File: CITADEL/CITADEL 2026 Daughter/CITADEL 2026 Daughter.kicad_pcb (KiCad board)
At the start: 2 copper layers, 36 x 36 mm, 4 parts

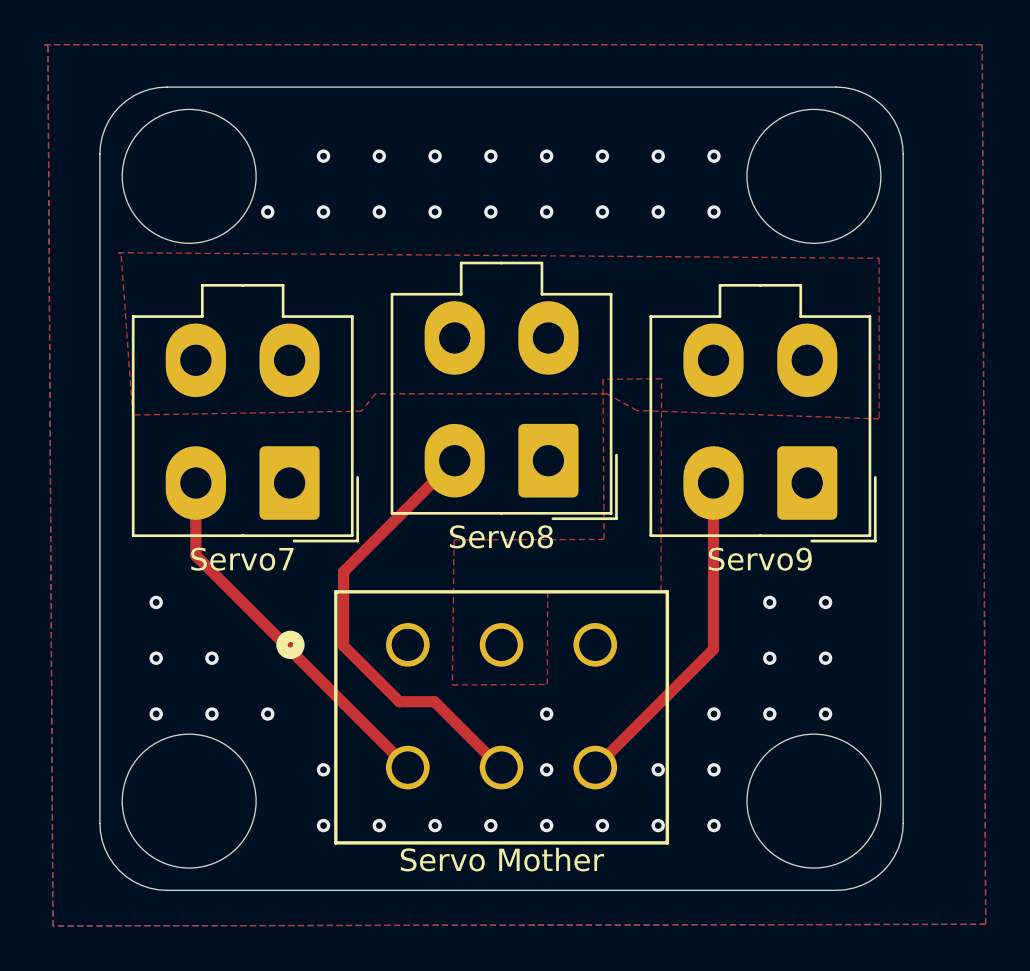
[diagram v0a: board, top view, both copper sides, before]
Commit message: Changed layout to support new linear actuators
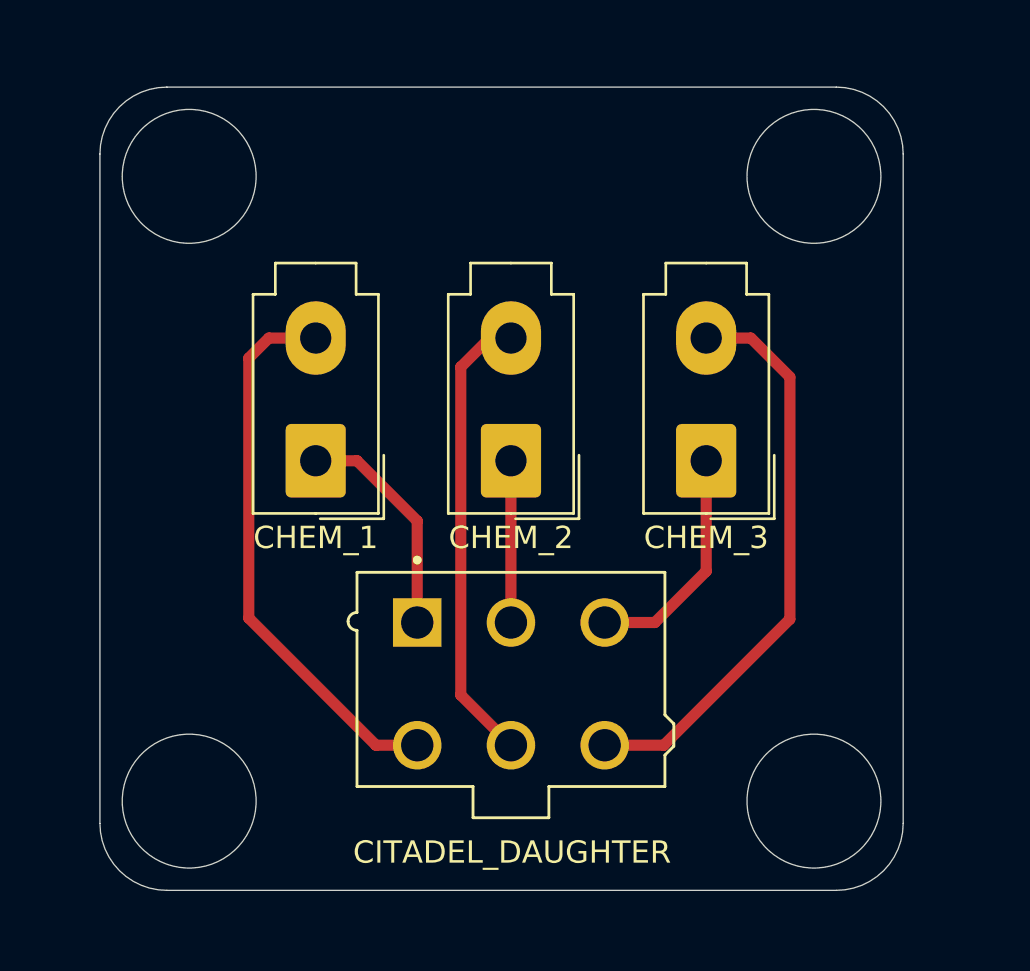
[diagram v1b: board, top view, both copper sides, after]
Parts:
- removed Servo7, Servo8, Servo9: Motor_Servo, Connector_Molex:Molex_Mini-Fit_Jr_5566-04A_2x02_P4.20mm_Vertical
- added CHEM_1: CHEM_1, Connector_Molex:Molex_Mini-Fit_Jr_5566-02A_2x01_P4.20mm_Vertical, F.Cu at (35.0, 38.4)
- added CHEM_2: CHEM_2, Connector_Molex:Molex_Mini-Fit_Jr_5566-02A_2x01_P4.20mm_Vertical, F.Cu at (43.7, 38.4)
- added CHEM_3: CHEM_3, Connector_Molex:Molex_Mini-Fit_Jr_5566-02A_2x01_P4.20mm_Vertical, F.Cu at (52.5, 38.4)
- CITADEL_DAUGHTER: renamed from Servo Mother; value Servo_Daughter -> CITADEL_DAUGHTER; footprint Jayse_Footprints:CONN_SD-5566-002_06_MOL -> Jayse_Footprints:MOLEX_0039281063
- moved CITADEL_DAUGHTER 4.87 mm to (43.7, 48.2)
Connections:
- CITADEL_DAUGHTER pad 1: unconnected-(J1-Pad1) -> /CHEM1_OUT1
- CITADEL_DAUGHTER pad 2: +5V -> /CHEM2_OUT1
- CITADEL_DAUGHTER pad 3: GND -> /CHEM3_OUT1
- CITADEL_DAUGHTER pad 4: /Servo7 -> /CHEM1_OUT2
- CITADEL_DAUGHTER pad 5: /Servo8 -> /CHEM2_OUT2
- CITADEL_DAUGHTER pad 6: /Servo9 -> /CHEM3_OUT2
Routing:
- net /CHEM3_OUT2: track 0.00 -> 26.0 mm
- net /CHEM1_OUT2: track 0.00 -> 24.9 mm
- net /CHEM2_OUT2: track 0.00 -> 20.7 mm
- net /Servo8: track 19.7 -> 0.00 mm
- net /Servo7: track 16.7 -> 0.00 mm
- net /Servo9: track 14.9 -> 0.00 mm
- net /CHEM3_OUT1: track 0.00 -> 10.5 mm
- net /CHEM1_OUT1: track 0.00 -> 10.2 mm
- net /CHEM2_OUT1: track 0.00 -> 7.25 mm
- net GND: vias 43 -> 0
- removed copper zone on F.Cu, net +5V
- removed copper zone on B.Cu, net GND
- removed copper zone on F.Cu, net GND

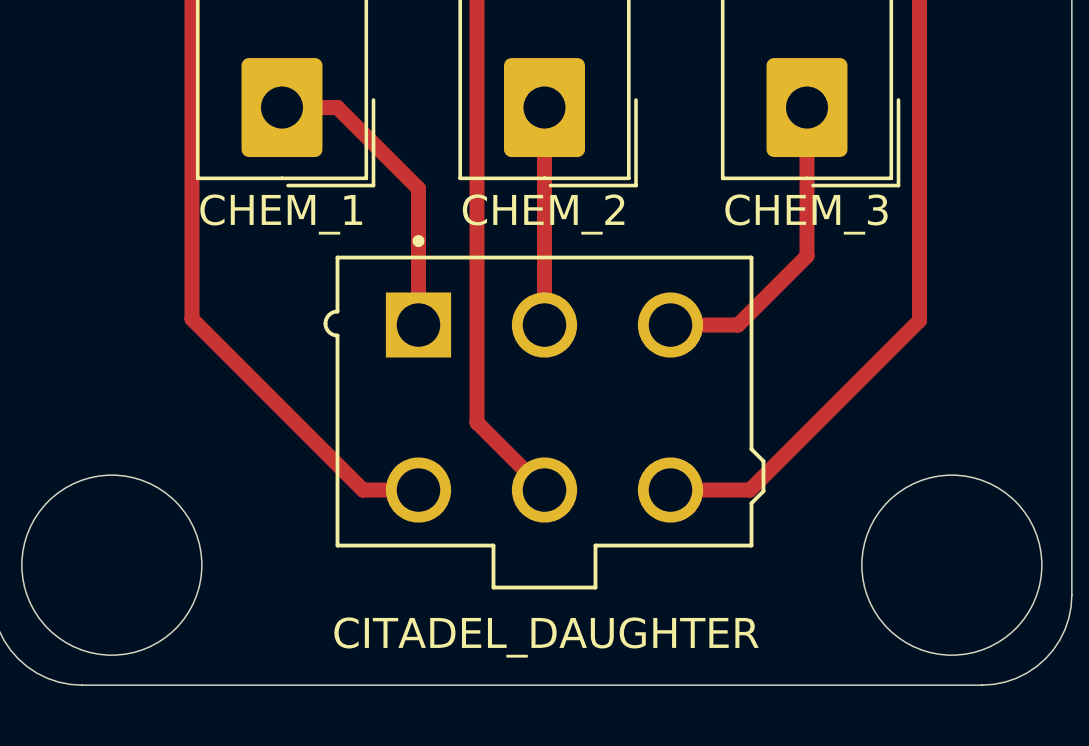
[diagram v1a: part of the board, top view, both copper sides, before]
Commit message: Updated reference names
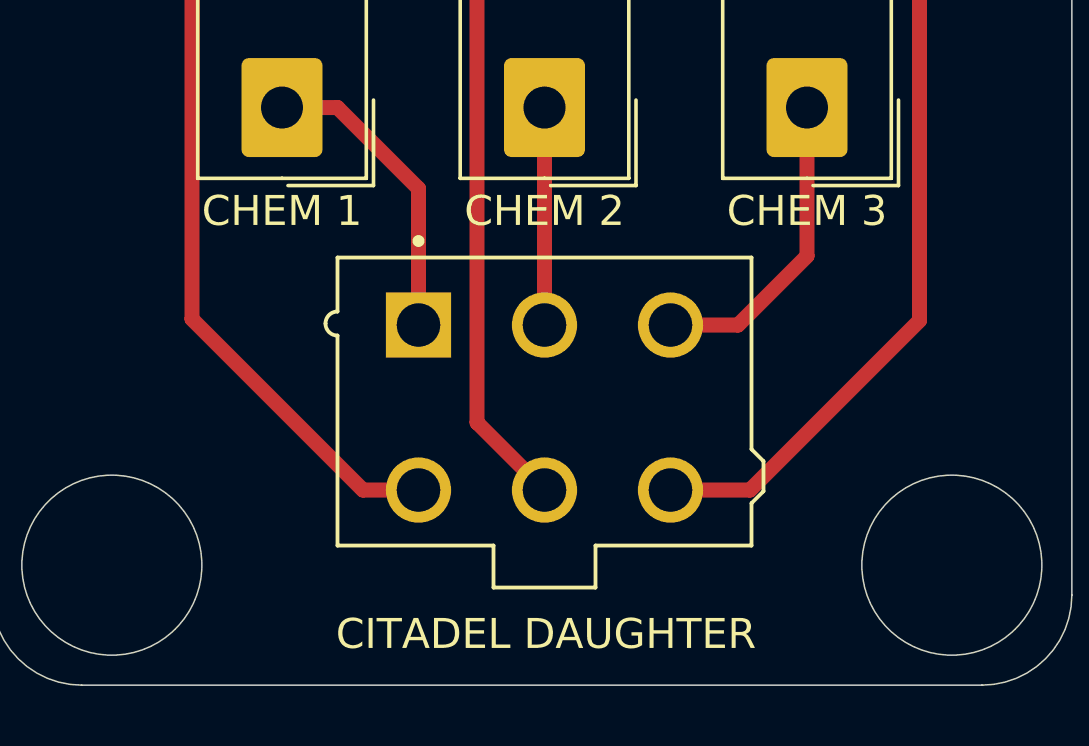
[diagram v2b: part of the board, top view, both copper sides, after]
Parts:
- CHEM 1: renamed from CHEM_1; value CHEM_1 -> CHEM 1
- CHEM 2: renamed from CHEM_2; value CHEM_2 -> CHEM 2
- CHEM 3: renamed from CHEM_3; value CHEM_3 -> CHEM 3
- CITADEL DAUGHTER: renamed from CITADEL_DAUGHTER; value CITADEL_DAUGHTER -> CITADEL DAUGHTER
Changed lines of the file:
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@@
 		(descr "Molex Mini-Fit Jr. Power Connectors, old mpn/engineering number: 5566-02A, example for new mpn: 39-28-x02x, 1 Pins per row, Mounting:  (http://www.molex.com/pdm_docs/sd/039281043_sd.pdf), generated with kicad-footprint-generator")
 		(tags "connector Molex Mini-Fit_Jr vertical")
-		(property "Reference" "CHEM_1"
+		(property "Reference" "CHEM 1"
 			(at 0 -3.45 0)
 			(layer "F.SilkS")
@@
 			)
 		)
-		(property "Value" "CHEM_1"
+		(property "Value" "CHEM 1"
 			(at 0 9.95 0)
 			(layer "F.Fab")
@@
 		(descr "Molex Mini-Fit Jr. Power Connectors, old mpn/engineering number: 5566-02A, example for new mpn: 39-28-x02x, 1 Pins per row, Mounting:  (http://www.molex.com/pdm_docs/sd/039281043_sd.pdf), generated with kicad-footprint-generator")
 		(tags "connector Molex Mini-Fit_Jr vertical")
-		(property "Reference" "CHEM_2"
+		(property "Reference" "CHEM 2"
 			(at 0 -3.45 0)
 			(layer "F.SilkS")
@@
 			)
 		)
-		(property "Value" "CHEM_2"
+		(property "Value" "CHEM 2"
 			(at 0 9.95 0)
 			(layer "F.Fab")
@@
 		(layer "F.Cu")
 		(at 43.7 48.2)
-		(property "Reference" "CITADEL_DAUGHTER"
+		(property "Reference" "CITADEL DAUGHTER"
 			(at 0.05 7.75 0)
 			(layer "F.SilkS")
@@
 			)
 		)
-		(property "Value" "CITADEL_DAUGHTER"
+		(property "Value" "CITADEL DAUGHTER"
 			(at 0 0.4625 0)
 			(layer "F.Fab")
@@
 		(descr "Molex Mini-Fit Jr. Power Connectors, old mpn/engineering number: 5566-02A, example for new mpn: 39-28-x02x, 1 Pins per row, Mounting:  (http://www.molex.com/pdm_docs/sd/039281043_sd.pdf), generated with kicad-footprint-generator")
 		(tags "connector Molex Mini-Fit_Jr vertical")
-		(property "Reference" "CHEM_3"
+		(property "Reference" "CHEM 3"
 			(at 0 -3.45 0)
 			(layer "F.SilkS")
@@
 			)
 		)
-		(property "Value" "CHEM_3"
+		(property "Value" "CHEM 3"
 			(at 0 9.95 0)
 			(layer "F.Fab")
@@
 		)
 	)
-	(gr_circle
-		(center 57.27868 25.65368)
-		(end 60.27868 25.65368)
+	(gr_arc
+		(start 25.27868 24.65368)
+		(mid 26.15736 22.53236)
+		(end 28.27868 21.65368)
 		(stroke
 			(width 0.05)
-			(type solid)
-		)
-		(fill no)
+			(type default)
+		)
+		(layer "Edge.Cuts")
+	)
+	(gr_line
+		(start 25.27868 54.65368)
+		(end 25.27868 24.65368)
+		(stroke
+			(width 0.05)
+			(type default)
+		)
+		(layer "Edge.Cuts")
+	)
+	(gr_line
+		(start 28.27868 21.65368)
+		(end 58.27868 21.65368)
+		(stroke
+			(width 0.05)
+			(type default)
+		)
 		(layer "Edge.Cuts")
 	)
@@
 	)
 	(gr_circle
-		(center 57.27868 53.65368)
-		(end 60.27868 53.65368)
+		(center 29.27868 25.65368)
+		(end 32.27868 25.65368)
 		(stroke
 			(width 0.05)
@@
 		)
 		(fill no)
-		(layer "Edge.Cuts")
-	)
-	(gr_arc
-		(start 61.27868 54.65368)
-		(mid 60.4 56.775)
-		(end 58.27868 57.65368)
-		(stroke
-			(width 0.05)
-			(type default)
-		)
-		(layer "Edge.Cuts")
-	)
-	(gr_arc
-		(start 25.27868 24.65368)
-		(mid 26.15736 22.53236)
-		(end 28.27868 21.65368)
-		(stroke
-			(width 0.05)
-			(type default)
-		)
 		(layer "Edge.Cuts")
 	)
@@
 		(layer "Edge.Cuts")
 	)
-	(gr_line
-		(start 28.27868 21.65368)
-		(end 58.27868 21.65368)
+	(gr_circle
+		(center 57.27868 25.65368)
+		(end 60.27868 25.65368)
 		(stroke
 			(width 0.05)
-			(type default)
-		)
-		(layer "Edge.Cuts")
-	)
-	(gr_line
-		(start 61.27868 24.65368)
-		(end 61.27868 54.65368)
-		(stroke
-			(width 0.05)
-			(type default)
-		)
-		(layer "Edge.Cuts")
-	)
-	(gr_line
-		(start 58.27868 57.65368)
-		(end 28.27868 57.65368)
-		(stroke
-			(width 0.05)
-			(type default)
-		)
+			(type solid)
+		)
+		(fill no)
 		(layer "Edge.Cuts")
 	)
 	(gr_circle
-		(center 29.27868 25.65368)
-		(end 32.27868 25.65368)
+		(center 57.27868 53.65368)
+		(end 60.27868 53.65368)
 		(stroke
 			(width 0.05)
@@
 	)
 	(gr_line
-		(start 25.27868 54.65368)
-		(end 25.27868 24.65368)
+		(start 58.27868 57.65368)
+		(end 28.27868 57.65368)
 		(stroke
 			(width 0.05)
@@
 		(layer "Edge.Cuts")
 	)
-	(gr_text "{\n  \"ViaStitching\": \"0.2\",\n  \"stitch_zone_0\": {\n    \"HSpacing\": \"2.5\",\n    \"VSpacing\": \"2.5\",\n    \"HOffset\": \"0\",\n    \"VOffset\": \"0\",\n    \"Clearance\": \"0.6\",\n    \"Randomize\": false\n  }\n}"
-		(at 0 0 0)
-		(layer "User.9")
-		(effects
-			(font
-				(size 1.27 1.27)
-			)
-			(justify left top)
-		)
+	(gr_line
+		(start 61.27868 24.65368)
+		(end 61.27868 54.65368)
+		(stroke
+			(width 0.05)
+			(type default)
+		)
+		(layer "Edge.Cuts")
+	)
+	(gr_arc
+		(start 61.27868 54.65368)
+		(mid 60.4 56.775)
+		(end 58.27868 57.65368)
+		(stroke
+			(width 0.05)
+			(type default)
+		)
+		(layer "Edge.Cuts")
 	)
 	(gr_text "{\n  \"ViaStitching\": \"0.2\",\n  \"stitch_zone_0\": {\n    \"HSpacing\": \"2.5\",\n    \"VSpacing\": \"2.5\",\n    \"HOffset\": \"0\",\n    \"VOffset\": \"0\",\n    \"Clearance\": \"0.6\",\n    \"Randomize\": false\n  }\n}"
-		(at 0 0 0)
-		(layer "User.9")
-		(effects
-			(font
-				(size 1.27 1.27)
-			)
-			(justify left top)
-		)
-	)
-	(gr_text "{\n  \"ViaStitching\": \"0.2\",\n  \"stitch_zone_0\": {\n    \"HSpacing\": \"2.5\",\n    \"VSpacing\": \"2.5\",\n    \"HOffset\": \"0\",\n    \"VOffset\": \"0\",\n    \"Clearance\": \"0.6\",\n    \"Randomize\": false\n  }\n}"
